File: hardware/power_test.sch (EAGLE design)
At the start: 53 parts, among them J10 USB-MICROA-AMPHENOL-10118192-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, J3 USB-MICROB-EDAC-690-005-299-0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, U1 DPDT-X2, U2 3.3V, U3 FT232RLSSOP, U4 MCP73831T-2ACI/OT, Y1 P-FET

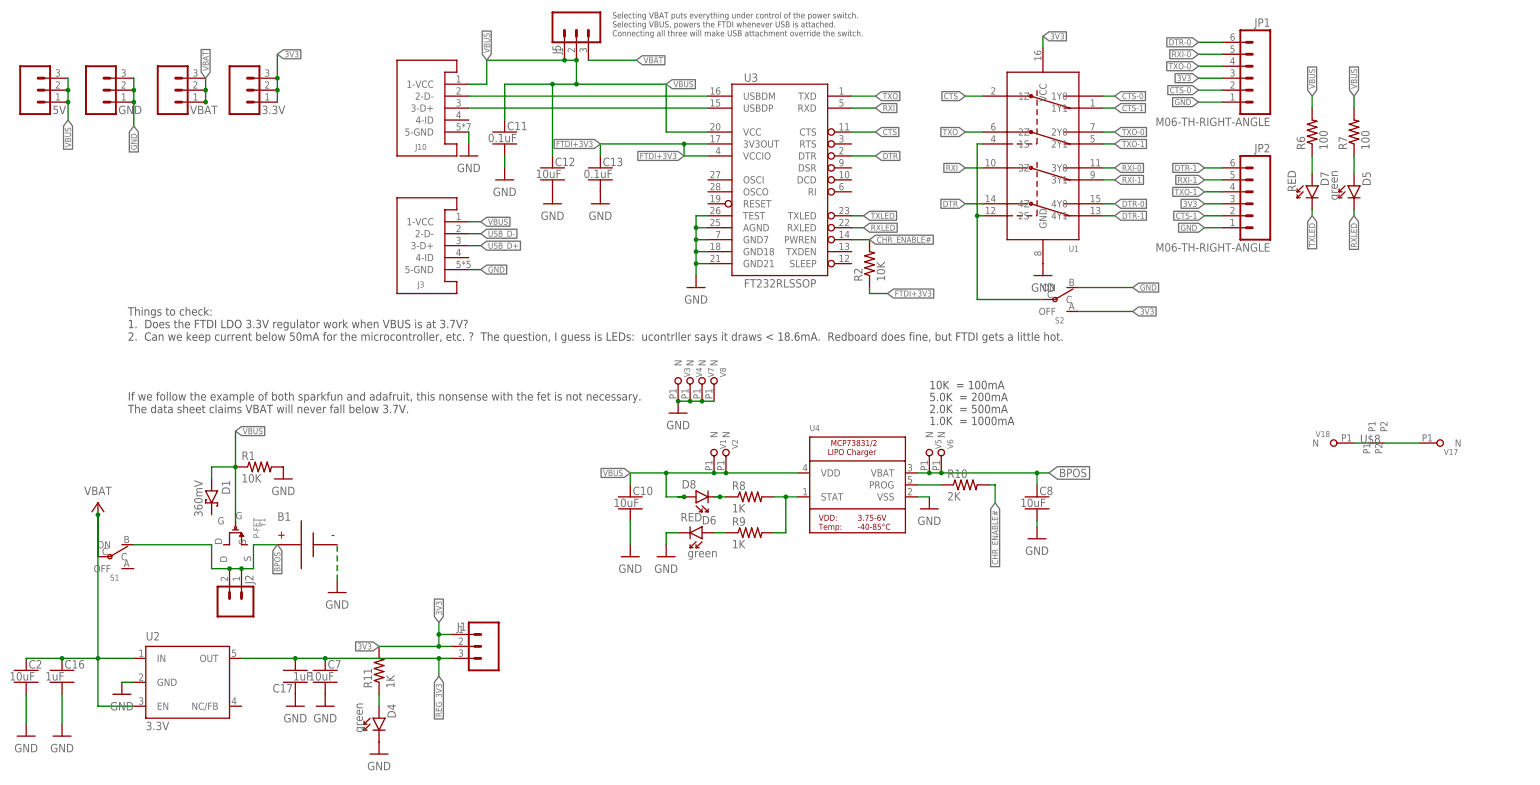
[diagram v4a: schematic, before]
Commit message: full breakout for battery charger.  remove voltage regulator.  Flip one FTDI port. New source switching scheme.  Remove various jumpers.  Fix Red LEDs
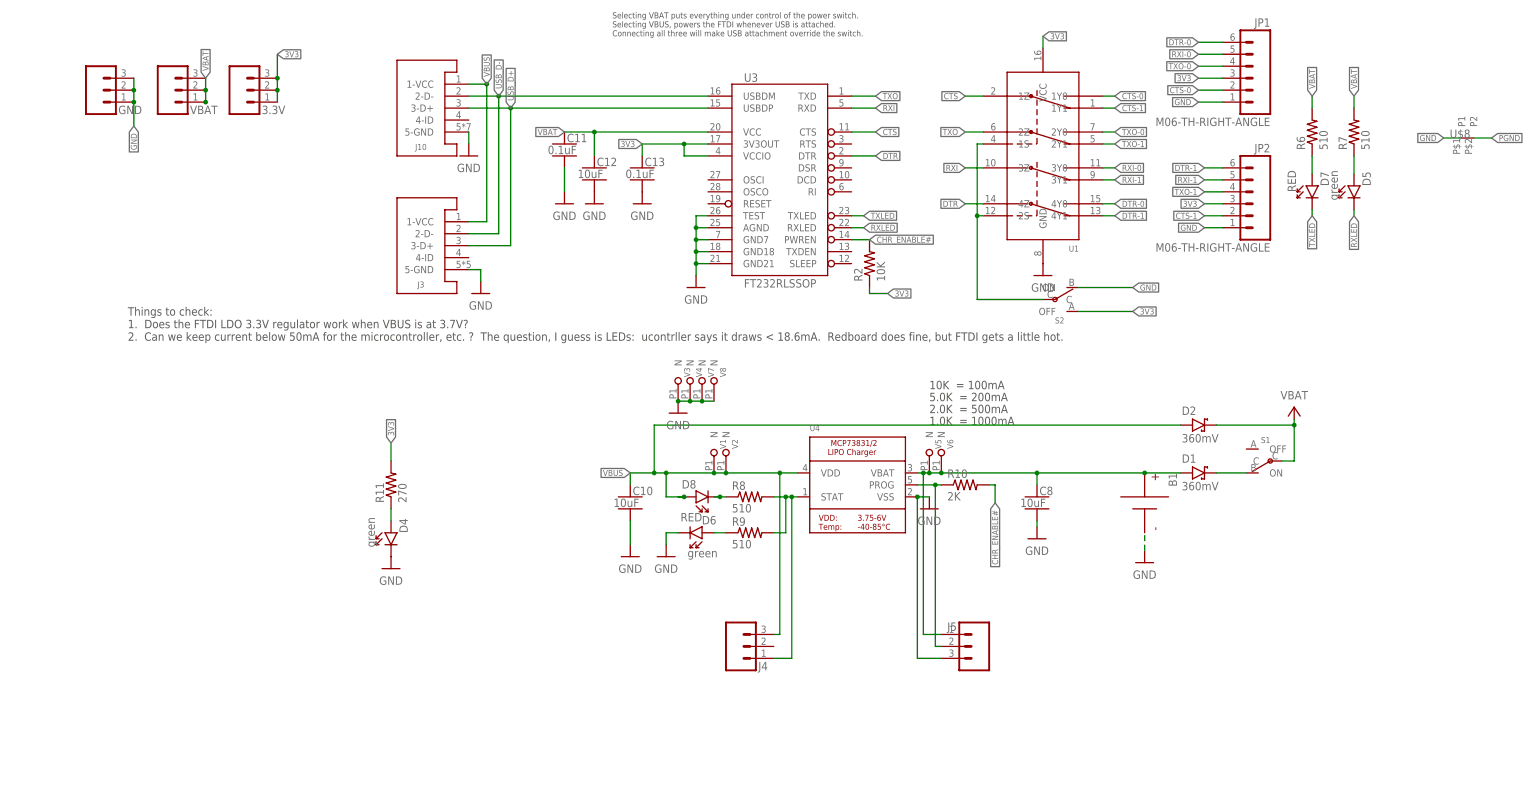
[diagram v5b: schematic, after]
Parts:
- removed 5V, J1: (no value), Components:HEADER-0.1IN-3POS-MALE
- removed C16, C17: 1uF, quadparts_prebuilt:CAPACITOR-NP_SMD-2012-0805_CERAMIC-1UF
- removed C2, C7: 10uF, quadparts_prebuilt:CAPACITOR-NP_SMD-2012-0805_CERAMIC-10UF
- removed J2: (no value), custom:MALE_HEADER_2POS-2X1-0.1IN
- removed R1: 10K, quadparts_prebuilt:RESISTOR_SMD-2012-0805-10K
- removed U2: 3.3V, quadparts_prebuilt:TPS73633-DBVT3V3
- removed V17, V18: (no value), quadparts_prebuilt:LOCKED-VIA-0.2
- removed Y1: P-FET, RemoteParts:P-FET
- added D2: 360mV, quadparts_prebuilt:DIODE-SCHOTTKY_SMD-SOD123-360MV
- added J4: (no value), Components:HEADER-0.1IN-3POS-MALE
- J5: PIN1 VBUS -> VBAT; PIN2 FTDI -> PROG; PIN3 VBAT -> VSS
- R11: value 1K -> 270; device quadparts_prebuilt:RESISTOR_SMD-2012-0805-1K -> quadparts_prebuilt:RESISTOR_SMD-2012-0805-270
- R6, R7: value 100 -> 510; device quadparts_prebuilt:RESISTOR_SMD-2012-0805-100 -> quadparts_prebuilt:RESISTOR_SMD-2012-0805-510
- R8, R9: value 1K -> 510; device quadparts_prebuilt:RESISTOR_SMD-2012-0805-1K -> quadparts_prebuilt:RESISTOR_SMD-2012-0805-510
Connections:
- removed net FTDI+3V3: C13.1, R2.1, U3.3V3OUT, U3.VCCIO
- removed net REG_3V3: C17.2, C7.1, J1.3, U2.OUT
- new net N$15: D1.C, S1.ON
- net 3V3: now also C13.1, R2.1, U3.3V3OUT, U3.VCCIO; no longer J1.1, J1.2
- net BPOS: now also D1.A, J5.1; no longer J2.1, J2.2, S1.ON
- net GND: now also J5.3; no longer C16.2, C17.1, C2.2, C7.2, R1.2, U2.GND, V18.N
- net N$11: now also J4.1
- net N$12: now also J5.2
- net PGND: no longer V17.N
- net VBAT: now also C11.1, C12.1, D2.C, R6.2, R7.2, U3.VCC; no longer C16.1, C2.1, J5.3, U2.EN, U2.IN
- net VBUS: now also D2.A, J4.3; no longer 5V.1, 5V.2, 5V.3, C11.1, C12.1, D1.A, J5.1, J5.2, R1.1, R6.2, R7.2, U3.VCC, Y1.G
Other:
- note removed: "If we follow the example of both sparkfun and adafruit, this nonsense with the fet is not necessary. The data sheet claims VBAT will never fall below 3.7V."
- moved on the sheet: B1, C11, C12, C13, D1, D4, J5, R11, S1, U$8

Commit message: small changes
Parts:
- added V10, V11, V9: (no value), quadparts_prebuilt:LOCKED-VIA-0.2
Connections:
- net 3V3: now also V11.N
- net VBAT: now also V10.N
- net VBUS: now also V9.N
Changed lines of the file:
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@@
 <class number="0" name="default" width="0" drill="0">
 </class>
-<class number="1" name="HIGH-I" width="0.508" drill="0">
+<class number="1" name="HIGH-I" width="0.381" drill="0">
 </class>
 <class number="2" name="RFSIG" width="0.4572" drill="0">
@@
 <attribute name="PIN3" value="VSS"/>
 </part>
+<part name="V9" library="quadparts_prebuilt" deviceset="LOCKED-VIA" device="-0.2"/>
+<part name="V10" library="quadparts_prebuilt" deviceset="LOCKED-VIA" device="-0.2"/>
+<part name="V11" library="quadparts_prebuilt" deviceset="LOCKED-VIA" device="-0.2"/>
 </parts>
 <sheets>
@@
 <instance part="J4" gate="G$1" x="157.48" y="135.89"/>
 <instance part="J5" gate="G$1" x="213.36" y="146.05" rot="R180"/>
+<instance part="V9" gate="G$1" x="165.1" y="187.96" rot="R90"/>
+<instance part="V10" gate="G$1" x="267.97" y="187.96" rot="R90"/>
+<instance part="V11" gate="G$1" x="86.36" y="181.61" rot="R180"/>
 </instances>
 <busses>
@@
 </segment>
 </net>
-<net name="3V3" class="0">
+<net name="3V3" class="1">
 <segment>
 <pinref part="U1" gate="G$1" pin="VCC"/>
@@
 <segment>
 <pinref part="R11" gate="G$1" pin="2"/>
-<wire x1="86.36" y1="180.34" x2="86.36" y2="184.15" width="0.1524" layer="91"/>
+<wire x1="86.36" y1="180.34" x2="86.36" y2="181.61" width="0.1524" layer="91"/>
 <label x="86.36" y="184.15" size="1.27" layer="95" rot="R90" xref="yes"/>
+<pinref part="V11" gate="G$1" pin="N"/>
+<wire x1="86.36" y1="181.61" x2="86.36" y2="184.15" width="0.1524" layer="91"/>
+<junction x="86.36" y="181.61"/>
 </segment>
 </net>
@@
 <junction x="278.13" y="187.96"/>
 <pinref part="D2" gate="G$1" pin="C"/>
-<wire x1="261.62" y1="187.96" x2="278.13" y2="187.96" width="0.1524" layer="91"/>
+<wire x1="261.62" y1="187.96" x2="267.97" y2="187.96" width="0.1524" layer="91"/>
+<pinref part="V10" gate="G$1" pin="N"/>
+<wire x1="267.97" y1="187.96" x2="278.13" y2="187.96" width="0.1524" layer="91"/>
+<junction x="267.97" y="187.96"/>
 </segment>
 </net>
@@
 <label x="137.16" y="177.8" size="1.27" layer="95" rot="R180" xref="yes"/>
 <wire x1="142.24" y1="177.8" x2="142.24" y2="187.96" width="0.1524" layer="91"/>
-<wire x1="142.24" y1="187.96" x2="254" y2="187.96" width="0.1524" layer="91"/>
+<wire x1="142.24" y1="187.96" x2="165.1" y2="187.96" width="0.1524" layer="91"/>
 <junction x="142.24" y="177.8"/>
 <pinref part="D2" gate="G$1" pin="A"/>
 <pinref part="J4" gate="G$1" pin="3"/>
+<wire x1="165.1" y1="187.96" x2="254" y2="187.96" width="0.1524" layer="91"/>
 <wire x1="168.91" y1="177.8" x2="168.91" y2="143.51" width="0.1524" layer="91"/>
 <wire x1="168.91" y1="143.51" x2="167.64" y2="143.51" width="0.1524" layer="91"/>
 <junction x="168.91" y="177.8"/>
-</segment>
-</net>
+<pinref part="V9" gate="G$1" pin="N"/>
+<junction x="165.1" y="187.96"/>
+</segment>
+</net>

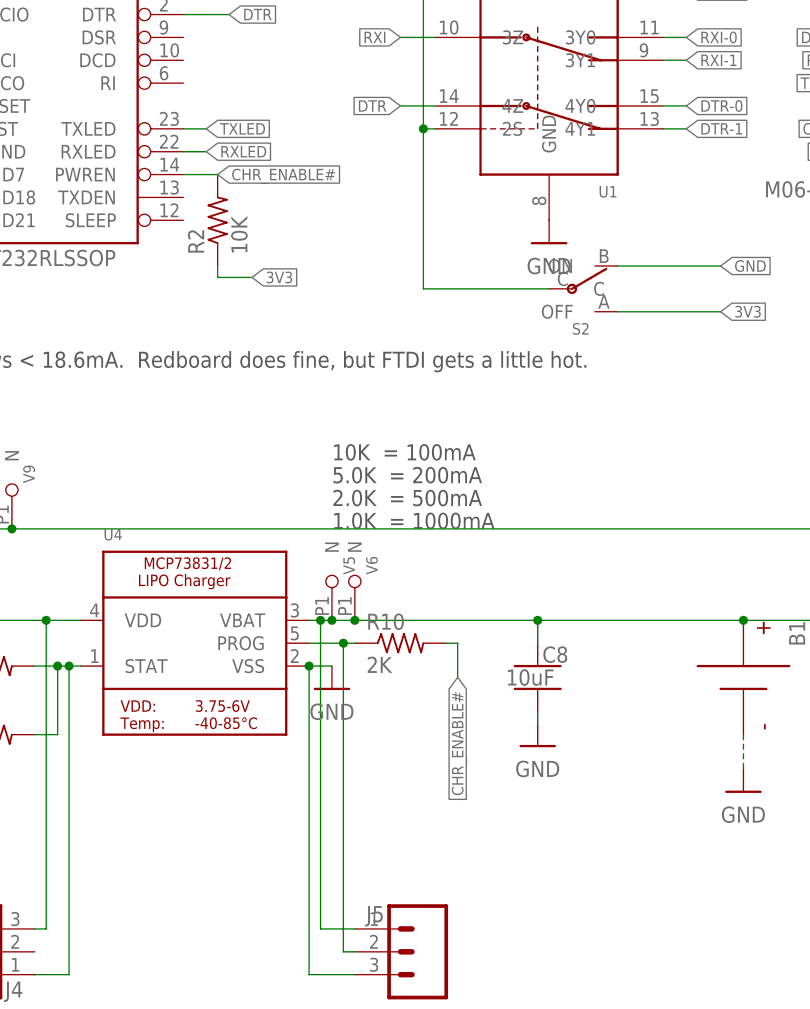
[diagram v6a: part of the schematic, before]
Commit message: Set charging current to 450mA
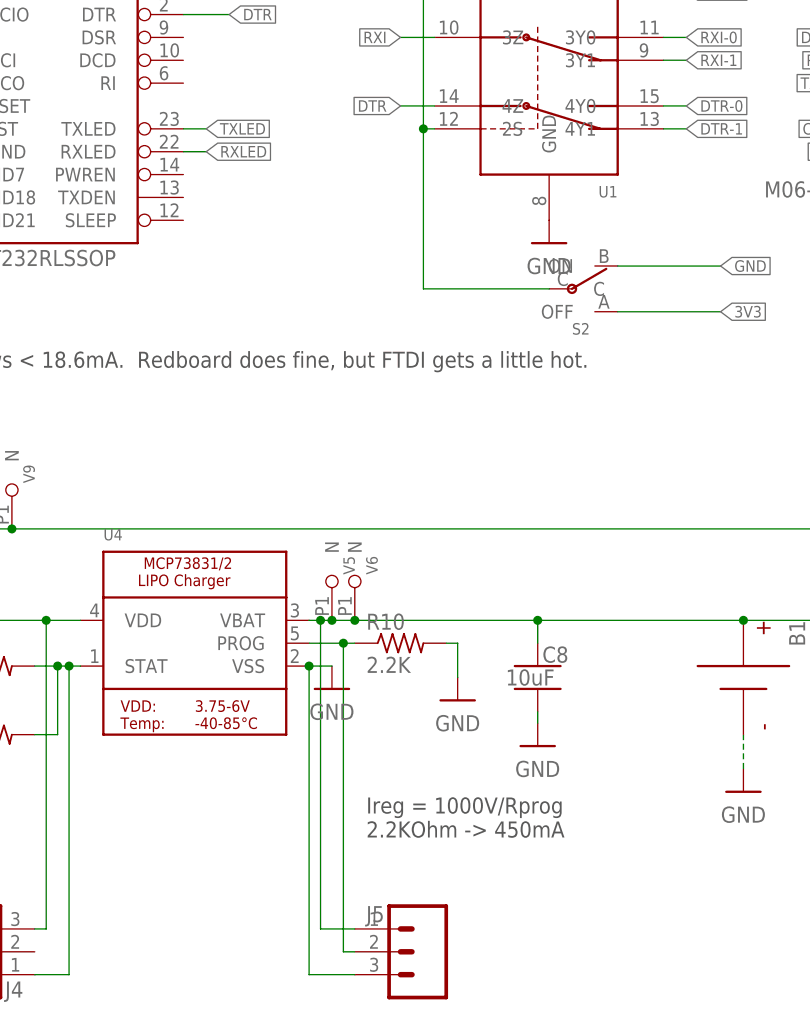
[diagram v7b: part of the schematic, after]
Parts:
- removed R2: 10K, quadparts_prebuilt:RESISTOR_SMD-2012-0805-10K
- R10: value 2K -> 2.2K; device quadparts_prebuilt:RESISTOR_SMD-2012-0805-2K -> quadparts_prebuilt:RESISTOR_SMD-2012-0805-2.2K
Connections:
- removed net CHR_ENABLE#: R10.2, R2.2, U3.PWREN
- net 3V3: no longer R2.1
- net GND: now also R10.2
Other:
- note added: "Ireg = 1000V/Rprog 2.2KOhm -> 450mA"
- note removed: "1.0K = 1000mA"
- note removed: "10K = 100mA"
- note removed: "2.0K = 500mA"
- note removed: "5.0K = 200mA"
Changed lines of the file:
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@@
 <part name="D8" library="RemoteParts" deviceset="DIODE-LED_" device="SMD-2012-0805-RED" value="RED"/>
 <part name="C8" library="quadparts_prebuilt" deviceset="CAPACITOR-NP_" device="SMD-2012-0805_CERAMIC-10UF" value="10uF"/>
-<part name="R10" library="quadparts_prebuilt" deviceset="RESISTOR_" device="SMD-2012-0805-2K" value="2K"/>
+<part name="R10" library="quadparts_prebuilt" deviceset="RESISTOR_" device="SMD-2012-0805-2.2K" value="2.2K"/>
 <part name="R11" library="quadparts_prebuilt" deviceset="RESISTOR_" device="SMD-2012-0805-270" value="270"/>
 <part name="V1" library="quadparts_prebuilt" deviceset="LOCKED-VIA" device="-0.2"/>
@@
 <part name="GND2" library="quadparts_prebuilt" deviceset="GND" device=""/>
 <part name="S2" library="RemoteParts" deviceset="POWER-SWITCH-MFS201N-9-Z" device="JS102011SAQN" value="POWER-SWITCH-MFS201N-9-ZJS102011SAQN"/>
-<part name="R2" library="quadparts_prebuilt" deviceset="RESISTOR_" device="SMD-2012-0805-10K" value="10K"/>
 <part name="D1" library="quadparts_prebuilt" deviceset="DIODE-SCHOTTKY_" device="SMD-SOD123-360MV" value="360mV"/>
 <part name="P+1" library="quadparts_prebuilt" deviceset="VBAT" device=""/>
@@
 <part name="V10" library="quadparts_prebuilt" deviceset="LOCKED-VIA" device="-0.2"/>
 <part name="V11" library="quadparts_prebuilt" deviceset="LOCKED-VIA" device="-0.2"/>
+<part name="U$1" library="quadparts_prebuilt" deviceset="GND" device=""/>
 </parts>
 <sheets>
 <sheet>
 <plain>
-<text x="200.66" y="195.58" size="1.778" layer="97">10K  = 100mA</text>
-<text x="200.66" y="193.04" size="1.778" layer="97">5.0K  = 200mA</text>
-<text x="200.66" y="190.5" size="1.778" layer="97">2.0K  = 500mA</text>
-<text x="200.66" y="187.96" size="1.778" layer="97">1.0K  = 1000mA</text>
+<text x="204.47" y="153.67" size="1.778" layer="97">Ireg = 1000V/Rprog
+2.2KOhm -&gt; 450mA</text>
 <text x="133.35" y="270.51" size="1.27" layer="97">Selecting VBAT puts everything under control of the power switch.
 Selecting VBUS, powers the FTDI whenever USB is attached.
@@
 <instance part="GND2" gate="1" x="224.79" y="219.71"/>
 <instance part="S2" gate="G$1" x="237.49" y="212.09"/>
-<instance part="R2" gate="G$1" x="187.96" y="222.25" rot="R90"/>
 <instance part="D1" gate="G$1" x="259.08" y="177.8"/>
 <instance part="P+1" gate="VCC" x="278.13" y="191.77"/>
@@
 <instance part="V10" gate="G$1" x="267.97" y="187.96" rot="R90"/>
 <instance part="V11" gate="G$1" x="86.36" y="181.61" rot="R180"/>
+<instance part="U$1" gate="1" x="214.63" y="168.91"/>
 </instances>
 <busses>
@@
 <label x="243.84" y="217.17" size="1.27" layer="95" xref="yes"/>
 </segment>
+<segment>
+<pinref part="R10" gate="G$1" pin="2"/>
+<wire x1="213.36" y1="175.26" x2="214.63" y2="175.26" width="0.1524" layer="91"/>
+<wire x1="214.63" y1="175.26" x2="214.63" y2="171.45" width="0.1524" layer="91"/>
+<pinref part="U$1" gate="1" pin="GND"/>
+</segment>
 </net>
 <net name="3V3" class="1">
@@
 <wire x1="148.59" y1="247.65" x2="148.59" y2="245.11" width="0.1524" layer="91"/>
 <junction x="148.59" y="247.65"/>
-</segment>
-<segment>
-<pinref part="R2" gate="G$1" pin="1"/>
-<wire x1="187.96" y1="217.17" x2="187.96" y2="215.9" width="0.1524" layer="91"/>
-<wire x1="187.96" y1="215.9" x2="191.77" y2="215.9" width="0.1524" layer="91"/>
-<label x="191.77" y="215.9" size="1.27" layer="95" xref="yes"/>
 </segment>
 <segment>
@@
 </segment>
 </net>
-<net name="CHR_ENABLE#" class="0">
-<segment>
-<pinref part="R10" gate="G$1" pin="2"/>
-<wire x1="213.36" y1="175.26" x2="214.63" y2="175.26" width="0.1524" layer="91"/>
-<wire x1="214.63" y1="175.26" x2="214.63" y2="171.45" width="0.1524" layer="91"/>
-<label x="214.63" y="171.45" size="1.27" layer="95" rot="R270" xref="yes"/>
-</segment>
-<segment>
-<pinref part="U3" gate="G$1" pin="PWREN"/>
-<wire x1="184.15" y1="227.33" x2="187.96" y2="227.33" width="0.1524" layer="91"/>
-<label x="187.96" y="227.33" size="1.27" layer="95" xref="yes"/>
-<pinref part="R2" gate="G$1" pin="2"/>
-</segment>
-</net>
